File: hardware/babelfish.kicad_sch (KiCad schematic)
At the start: 95 parts, among them J1 Shifter Power, J2 SWD, J3 DE9 Female, J4 USB_A, Q1 BSS138, SW1 TS342A2P-WZ, SW2 TS342A2P-WZ, SW3 SK12D07VG5_C3020419, U1 RP2040, U10 74HC4052PW,118, U11 MAX3232IDR, U12 AP2191WG-7, U2 TPS2113ADRBR, U3 GT-USB-7010ASV, U4 W25Q128JVS, U5 TPMCP1703T-5002E_CB, U6 TPMCP1703T-3302E_CB, U7 74HC4052PW,118, U8 74HC4052PW,118, U9 74HC4052PW,118, X1 X322512MSB4SI

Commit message: hw v0.3
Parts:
- J3: symbol Connector:DE9_Receptacle -> Connector:DE9_Receptacle_2Holes
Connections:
- net GND: now also J3.10 (PAD), J3.11 (PAD), U10.11 (1Y3), U7.4 (2Y3), U8.11 (1Y3), U9.4 (2Y3)
- net GPIO24: now reaches U1.36 (GPIO24)
- net GPIO25: now reaches U1.37 (GPIO25)
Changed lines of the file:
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@@
   (junction (at 165.735 31.115) (diameter 0) (color 0 0 0 0)
   )
+  (junction (at 139.065 193.675) (diameter 0) (color 0 0 0 0)
+  )
   (junction (at 369.57 46.99) (diameter 0) (color 0 0 0 0)
   )
@@
   (junction (at 149.225 51.435) (diameter 0) (color 0 0 0 0)
   )
+  (junction (at 192.405 189.865) (diameter 0) (color 0 0 0 0)
+  )
   (junction (at 195.58 226.06) (diameter 0) (color 0 0 0 0)
   )
@@
   (junction (at 265.43 194.945) (diameter 0) (color 0 0 0 0)
   )
+  (junction (at 192.405 220.98) (diameter 0) (color 0 0 0 0)
+  )
   (junction (at 340.36 184.15) (diameter 0) (color 0 0 0 0)
   )
@@
   )
   (no_connect (at 187.325 125.095))
-  (no_connect (at 198.12 187.325))
-  (no_connect (at 223.52 187.325))
   (no_connect (at 187.325 99.695))
-  (no_connect (at 172.085 142.875))
+  (no_connect (at 223.52 218.44))
   (no_connect (at 187.325 92.075))
   (no_connect (at 187.325 94.615))
   (no_connect (at 267.97 187.325))
-  (no_connect (at 223.52 218.44))
+  (no_connect (at 187.325 142.875))
+  (no_connect (at 187.325 145.415))
+  (no_connect (at 223.52 187.325))
+  (no_connect (at 187.325 155.575))
   (no_connect (at 187.325 122.555))
-  (no_connect (at 198.12 218.44))
-  (no_connect (at 293.37 187.325))
-  (no_connect (at 172.085 145.415))
+  (no_connect (at 187.325 153.035))
   (no_connect (at 267.97 218.44))
-  (no_connect (at 293.37 218.44))
+  (no_connect (at 187.325 150.495))
+  (no_connect (at 187.325 158.115))
   (no_connect (at 187.325 137.795))
   (wire (pts (xy 172.085 132.715) (xy 187.325 132.715))
@@
     (stroke (width 0) (type default))
   )
+  (wire (pts (xy 131.445 193.675) (xy 131.445 195.58))
+    (stroke (width 0) (type default))
+  )
   (wire (pts (xy 295.91 226.06) (xy 295.91 227.965))
     (stroke (width 0) (type default))
@@
     (stroke (width 0) (type default))
   )
+  (wire (pts (xy 141.605 195.58) (xy 141.605 193.675))
+    (stroke (width 0) (type default))
+  )
   (wire (pts (xy 172.085 74.295) (xy 183.515 74.295))
     (stroke (width 0) (type default))
@@
     (stroke (width 0) (type default))
   )
+  (wire (pts (xy 293.37 187.325) (xy 306.705 187.325))
+    (stroke (width 0) (type default))
+  )
   (wire (pts (xy 340.36 193.04) (xy 340.36 194.31))
     (stroke (width 0) (type default))
@@
     (stroke (width 0) (type default))
   )
+  (wire (pts (xy 172.085 142.875) (xy 187.325 142.875))
+    (stroke (width 0) (type default))
+  )
   (wire (pts (xy 156.845 220.98) (xy 156.845 224.155))
     (stroke (width 0) (type default))
@@
     (stroke (width 0) (type default))
   )
+  (wire (pts (xy 139.065 193.675) (xy 139.065 196.85))
+    (stroke (width 0) (type default))
+  )
   (wire (pts (xy 316.865 97.79) (xy 323.215 97.79))
     (stroke (width 0) (type default))
@@
     (stroke (width 0) (type default))
   )
+  (wire (pts (xy 192.405 187.325) (xy 192.405 189.865))
+    (stroke (width 0) (type default))
+  )
   (wire (pts (xy 332.105 29.21) (xy 332.105 31.115))
     (stroke (width 0) (type default))
@@
     (stroke (width 0) (type default))
   )
+  (wire (pts (xy 139.065 193.675) (xy 131.445 193.675))
+    (stroke (width 0) (type default))
+  )
   (wire (pts (xy 186.69 210.82) (xy 198.12 210.82))
     (stroke (width 0) (type default))
   )
+  (wire (pts (xy 198.12 187.325) (xy 192.405 187.325))
+    (stroke (width 0) (type default))
+  )
   (wire (pts (xy 165.735 55.245) (xy 165.735 56.515))
     (stroke (width 0) (type default))
@@
     (stroke (width 0) (type default))
   )
+  (wire (pts (xy 192.405 218.44) (xy 192.405 220.98))
+    (stroke (width 0) (type default))
+  )
   (wire (pts (xy 153.67 257.81) (xy 153.67 259.08))
     (stroke (width 0) (type default))
@@
     (stroke (width 0) (type default))
   )
+  (wire (pts (xy 172.085 145.415) (xy 187.325 145.415))
+    (stroke (width 0) (type default))
+  )
   (wire (pts (xy 332.105 45.72) (xy 343.535 45.72))
     (stroke (width 0) (type default))
@@
     (stroke (width 0) (type default))
   )
+  (wire (pts (xy 141.605 193.675) (xy 139.065 193.675))
+    (stroke (width 0) (type default))
+  )
   (wire (pts (xy 172.085 127.635) (xy 194.31 127.635))
     (stroke (width 0) (type default))
@@
     (stroke (width 0) (type default))
   )
+  (wire (pts (xy 198.12 218.44) (xy 192.405 218.44))
+    (stroke (width 0) (type default))
+  )
   (wire (pts (xy 172.085 84.455) (xy 187.325 84.455))
     (stroke (width 0) (type default))
@@
     (stroke (width 0) (type default))
   )
+  (wire (pts (xy 293.37 218.44) (xy 306.705 218.44))
+    (stroke (width 0) (type default))
+  )
   (wire (pts (xy 93.98 225.425) (xy 93.98 222.885))
     (stroke (width 0) (type default))
@@
     (effects (font (size 1.27 1.27)) (justify right bottom))
   )
+  (label "GPIO24" (at 187.325 142.875 180) (fields_autoplaced)
+    (effects (font (size 1.27 1.27)) (justify right bottom))
+  )
   (label "SWD" (at 70.485 169.545 0) (fields_autoplaced)
     (effects (font (size 1.27 1.27)) (justify left bottom))
@@
     (effects (font (size 1.27 1.27)) (justify right bottom))
   )
+  (label "GPIO25" (at 187.325 145.415 180) (fields_autoplaced)
+    (effects (font (size 1.27 1.27)) (justify right bottom))
+  )
   (label "LED_PWR" (at 187.325 97.155 180) (fields_autoplaced)
     (effects (font (size 1.27 1.27)) (justify right bottom))
@@
     )
   )
+  (symbol (lib_id "power:GND") (at 131.445 195.58 0) (unit 1)
+    (in_bom yes) (on_board yes) (dnp no) (fields_autoplaced)
+    (property "Reference" "#PWR066" (at 131.445 201.93 0)
+      (effects (font (size 1.27 1.27)) hide)
+    )
+    (property "Value" "GND" (at 131.445 200.66 0)
+      (effects (font (size 1.27 1.27)))
+    )
+    (property "Footprint" "" (at 131.445 195.58 0)
+      (effects (font (size 1.27 1.27)) hide)
+    )
+    (property "Datasheet" "" (at 131.445 195.58 0)
+      (effects (font (size 1.27 1.27)) hide)
+    )
+    (pin "1")
+    (instances
+      (project "babelfish"
+        (path "/25a7582e-3999-4fda-9acd-cd1e305548b6"
+          (reference "#PWR066") (unit 1)
+        )
+      )
+    )
+  )
+  (symbol (lib_id "power:GND") (at 306.705 187.325 0) (unit 1)
+    (in_bom yes) (on_board yes) (dnp no) (fields_autoplaced)
+    (property "Reference" "#PWR064" (at 306.705 193.675 0)
+      (effects (font (size 1.27 1.27)) hide)
+    )
+    (property "Value" "GND" (at 306.705 191.77 0)
+      (effects (font (size 1.27 1.27)))
+    )
+    (property "Footprint" "" (at 306.705 187.325 0)
+      (effects (font (size 1.27 1.27)) hide)
+    )
+    (property "Datasheet" "" (at 306.705 187.325 0)
+      (effects (font (size 1.27 1.27)) hide)
+    )
+    (pin "1")
+    (instances
+      (project "babelfish"
+        (path "/25a7582e-3999-4fda-9acd-cd1e305548b6"
+          (reference "#PWR064") (unit 1)
+        )
+      )
+    )
+  )
   (symbol (lib_id "LCSC:TPS2113ADRBR") (at 302.895 46.99 0) (unit 1)
     (in_bom yes) (on_board yes) (dnp no)
@@
     )
   )
+  (symbol (lib_id "power:GND") (at 306.705 218.44 0) (unit 1)
+    (in_bom yes) (on_board yes) (dnp no) (fields_autoplaced)
+    (property "Reference" "#PWR065" (at 306.705 224.79 0)
+      (effects (font (size 1.27 1.27)) hide)
+    )
+    (property "Value" "GND" (at 306.705 223.52 0)
+      (effects (font (size 1.27 1.27)))
+    )
+    (property "Footprint" "" (at 306.705 218.44 0)
+      (effects (font (size 1.27 1.27)) hide)
+    )
+    (property "Datasheet" "" (at 306.705 218.44 0)
+      (effects (font (size 1.27 1.27)) hide)
+    )
+    (pin "1")
+    (instances
+      (project "babelfish"
+        (path "/25a7582e-3999-4fda-9acd-cd1e305548b6"
+          (reference "#PWR065") (unit 1)
+        )
+      )
+    )
+  )
   (symbol (lib_id "power:+3V3") (at 340.36 228.6 0) (unit 1)
     (in_bom yes) (on_board yes) (dnp no) (fields_autoplaced)
@@
     )
   )
-  (symbol (lib_id "Connector:DE9_Receptacle") (at 141.605 210.82 180) (unit 1)
+  (symbol (lib_id "Connector:DE9_Receptacle_2Holes") (at 141.605 210.82 180) (unit 1)
     (in_bom yes) (on_board yes) (dnp no) (fields_autoplaced)
-    (property "Reference" "J3" (at 141.605 193.04 0)
-      (effects (font (size 1.27 1.27)))
+    (property "Reference" "J3" (at 135.89 209.55 0)
+      (effects (font (size 1.27 1.27)) (justify left))
     )
-    (property "Value" "DE9 Female" (at 141.605 195.58 0)
-      (effects (font (size 1.27 1.27)))
+    (property "Value" "DE9 Female" (at 135.89 212.09 0)
+      (effects (font (size 1.27 1.27)) (justify left))
     )
     (property "Footprint" "lcsc:DSUB-TH_DMR-9S" (at 141.605 210.82 0)
@@
     )
     (pin "1")
+    (pin "10")
+    (pin "11")
     (pin "2")
     (pin "3")

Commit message: WIP fixing the mux/demux
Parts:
- removed U10, U8: 74HC4052PW,118, lcsc:TSSOP-16_L5.0-W4.4-P0.65-LS6.4-BL, symbol LCSC:74HC4052PW,118
- added C32, C33, C34: C_Small, symbol Device:C_Small
- added C35: Xu, symbol Device:C_Small
- added D4: D_Schottky_Small, symbol Device:D_Schottky_Small
- added DIP1: KF1001-08P-R0-GL-DFT-01B, lcsc:SW-TH_16P-L21.9-W9.9-P2.54-LS7.6, symbol LCSC:KF1001-08P-R0-GL-DFT-01B
- added L1: L_Small, symbol Device:L_Small
- added R29: R_Small, symbol Device:R_Small
- added R30, R31: XK, symbol Device:R_Small
- added U9: LMR14020SDDAR, lcsc:HSOP-8_L5.0-W4.0-P1.27-LS6.2-BL-EP, symbol LCSC:LMR14020SDDAR
- renumbered U9 to U8
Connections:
- net GND: now also U7.11 (1Y3), U8.11 (1Y3), C32.1, C34.2, C35.1, D4.2 (A), R29.1, R31.2, U9.7 (GND), U9.9 (EPAD)
- net RX_A: now also U7.3 (2Z)
- net RX_A_1Y1: now also U7.5 (2Y1)
- net RX_A_1Y2: now also U7.2 (2Y2)
- net RX_A_2Y1: now also DIP1.3 (PIN3)
- net RX_A_2Y2: now also DIP1.4 (PIN4)
- net RX_A_CONN: now also U7.1 (2Y0), DIP1.13 (PIN13), DIP1.14 (PIN14)
- net RX_B: now also U8.3 (2Z)
- net RX_B_1Y1: now also U8.5 (2Y1)
- net RX_B_1Y2: now also U8.2 (2Y2)
- net RX_B_2Y1: now also DIP1.7 (PIN7)
- net RX_B_2Y2: now also DIP1.8 (PIN8)
- net RX_B_CONN: now also U8.1 (2Y0), DIP1.10 (PIN10), DIP1.9 (PIN9)
- net TX_A_2Y1: now also DIP1.1 (PIN1); no longer U7.5 (2Y1)
- net TX_A_2Y2: now also DIP1.2 (PIN2); no longer U7.2 (2Y2)
- net TX_A_CONN: now also U7.12 (1Y0), DIP1.15 (PIN15), DIP1.16 (PIN16); no longer U7.3 (2Z)
- net TX_B_2Y1: now also DIP1.5 (PIN5); no longer U8.5 (2Y1)
- net TX_B_2Y2: now also DIP1.6 (PIN6); no longer U8.2 (2Y2)
- net TX_B_CONN: now also U8.12 (1Y0), DIP1.11 (PIN11), DIP1.12 (PIN12); no longer U8.3 (2Z)
- removed net TX_A_Y0_THRU: U7.1 (2Y0), U7.12 (1Y0)
- removed net TX_B_Y0_THRU: U8.1 (2Y0), U8.12 (1Y0)
- new net: C33.1, D4.1 (K), L1.1, U9.8 (SW)
- new net: C34.1, L1.2, R30.1
- new net: R30.2, R31.1, U9.5 (FB)
- new net: C33.2, U9.1 (BOOT)
- new net: C32.2, U9.2 (VIN), U9.3 (EN)
- new net: R29.2, U9.4 (RT/SYNC)
- new net: C35.2, U9.6 (SS)
- no-connect marks 16 -> 12
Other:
- note added: "MCU Signals"
- note added: "Output Signals"
- note added: "Signal Sel"
- note removed: "Signal Mux/Demux"

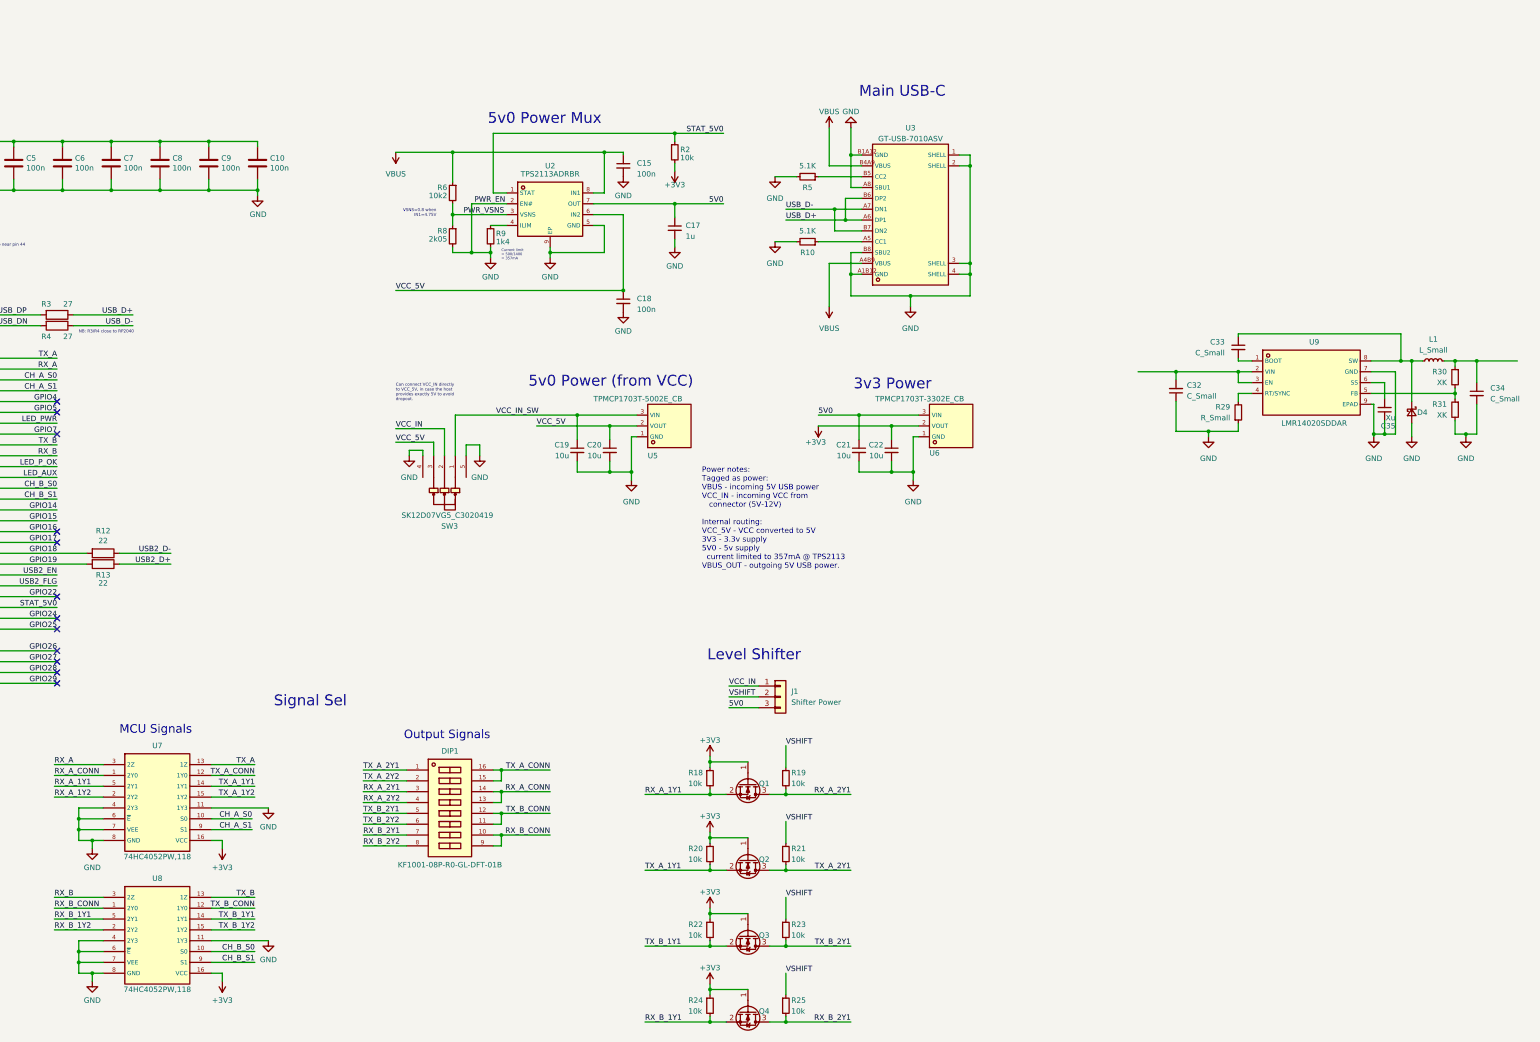
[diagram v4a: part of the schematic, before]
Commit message: more dip switch replacements
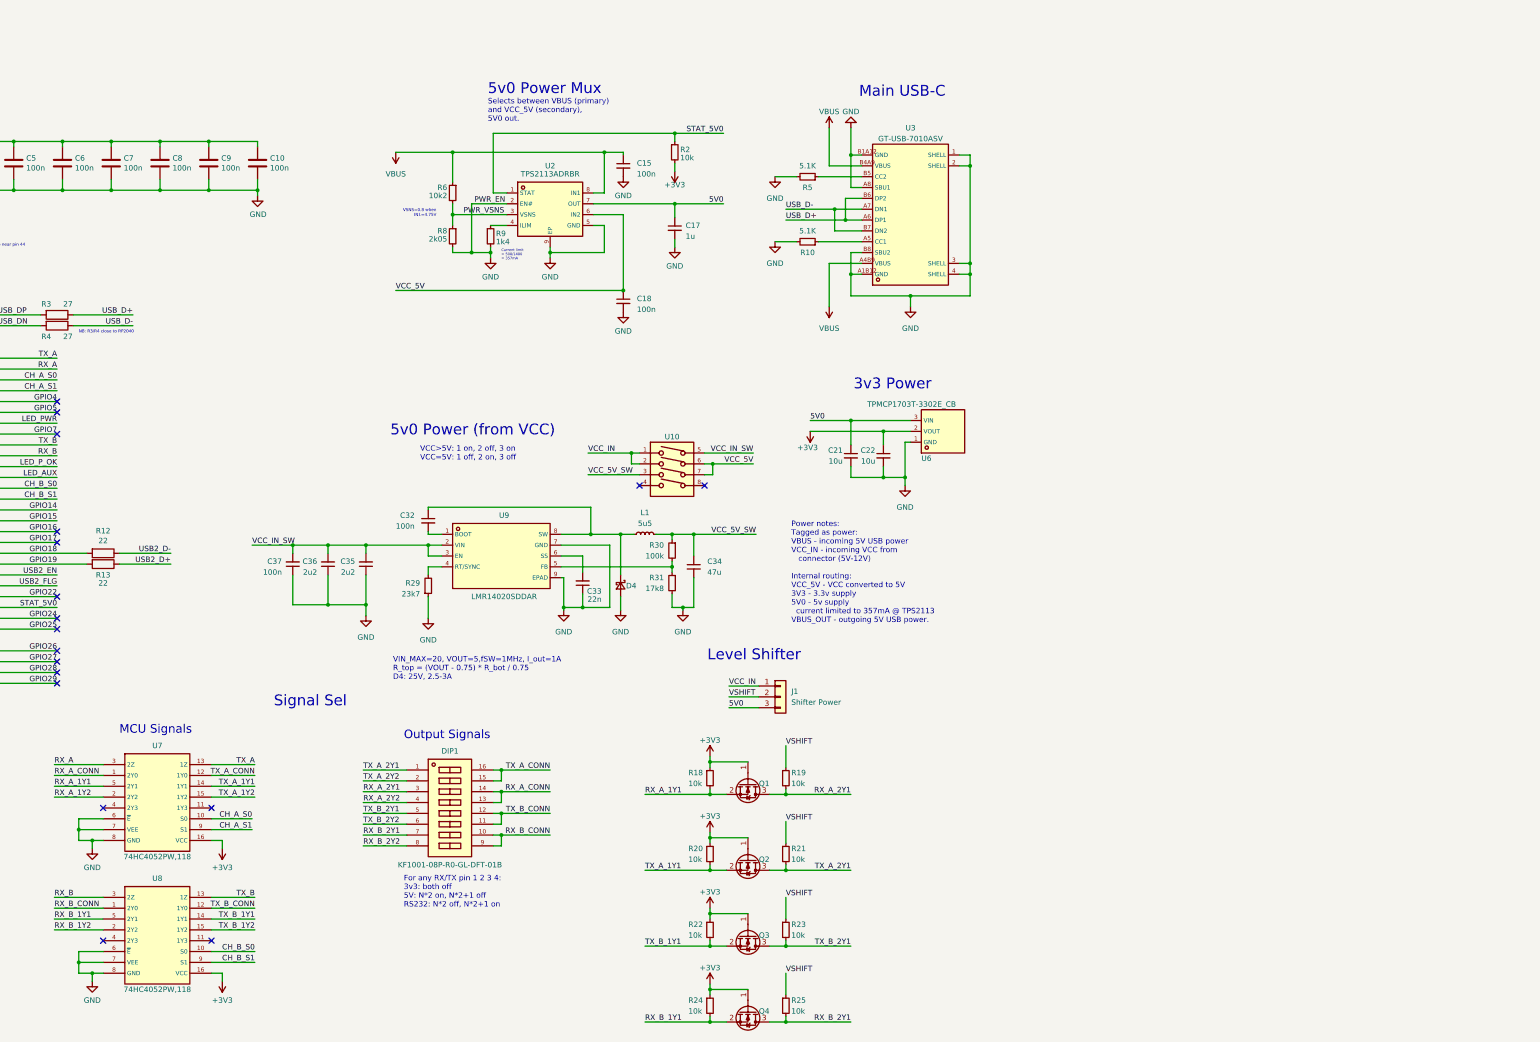
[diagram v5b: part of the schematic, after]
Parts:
- removed C19, C20: 10u, Capacitor_SMD:C_0805_2012Metric, symbol Device:C_Small
- removed SW3: SK12D07VG5_C3020419, lcsc:SW-TH_SHOU_SK12D07VG5, symbol LCSC:SK12D07VG5_C3020419
- removed U5: TPMCP1703T-5002E_CB, lcsc:SOT-23-3_L2.9-W1.6-P1.90-LS2.8-BR, symbol LCSC:TPMCP1703T-5002E_CB
- added C36: 2u2, Capacitor_SMD:C_1206_3216Metric, symbol Device:C_Small
- added C37: 100n, Capacitor_SMD:C_0402_1005Metric, symbol Device:C_Small
- added U10: DSWB04LHGET, lcsc:SW-TH_DSWB04LHGET, symbol LCSC:DSWB04LHGET
- C32: renamed from C33; value C_Small -> 100n; footprint (none) -> Capacitor_SMD:C_0402_1005Metric; Notes (none) -> 25V+ X7R
- C33: renamed from C35; value Xu -> 22n; footprint (none) -> Capacitor_SMD:C_0402_1005Metric
- C34: value C_Small -> 47u; footprint (none) -> Capacitor_SMD:C_0805_2012Metric
- C35: renamed from C32; value C_Small -> 2u2; footprint (none) -> Capacitor_SMD:C_1206_3216Metric; Notes (none) -> X7R 100V
- D4: footprint (none) -> Diode_SMD:D_SMA
- L1: value L_Small -> 5u5
- R29: value R_Small -> 23k7
- R30: value XK -> 100k
- R31: value XK -> 17k8
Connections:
- net GND: now also C36.1, C37.1; no longer U7.11 (1Y3), U7.4 (2Y3), U8.11 (1Y3), U8.4 (2Y3)
- net VCC_5V: now also U10.6, U10.7
- net VCC_IN: now also U10.1, U10.2
- net VCC_IN_SW: now also C35.2, U9.2 (VIN), U9.3 (EN), C36.2, C37.2, U10.5
- net VCC_5V_SW: now reaches C34.1, L1.2, R30.1
- net VCC_5V_SW: now also U10.3
- no-connect marks 12 -> 18
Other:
- note added: "For any RX/TX pin 1 2 3 4: 3v3: both off 5V: N*2 on, N*2+1 off RS232: N*2 off, N*2+1 on"
- note added: "Selects between VBUS (primary) and VCC_5V (secondary), 5V0 out."
- note added: "VCC>5V: 1 on, 2 off, 3 on VCC=5V: 1 off, 2 on, 3 off"
- note added: "VIN_MAX=20, VOUT=5,fSW=1MHz, I_out=1A R_top = (VOUT - 0.75) * R_bot / 0.75 D4: 25V, 2.5-3A"
- note removed: "Can connect VCC_IN directly to VCC_5V, in case the host provides exactly 5V to avoid dropout."
- moved on the sheet: C21, C22, C32, C33, C34, C35, D4, L1, R29, R30, R31, U6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
